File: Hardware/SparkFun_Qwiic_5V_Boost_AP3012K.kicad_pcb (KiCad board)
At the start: 2 copper layers, 25.4 x 25.4 mm, 55 parts, among them J1 Qwiic_RA, J2 Qwiic_RA, J3 Conn_01x06, Q1 BSS138, Q2 BSS138, U5 AP3012

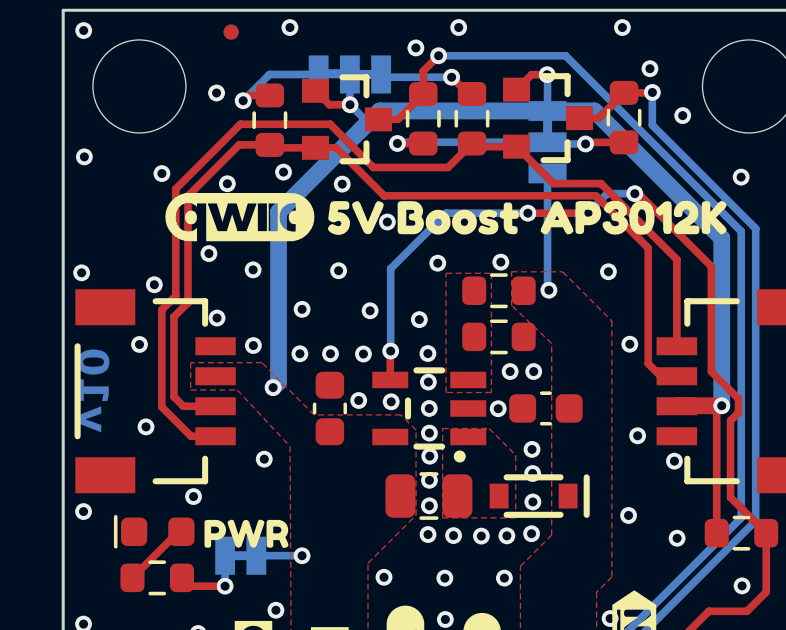
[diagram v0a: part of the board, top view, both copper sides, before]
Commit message: silk adjustments - add flame logo to top
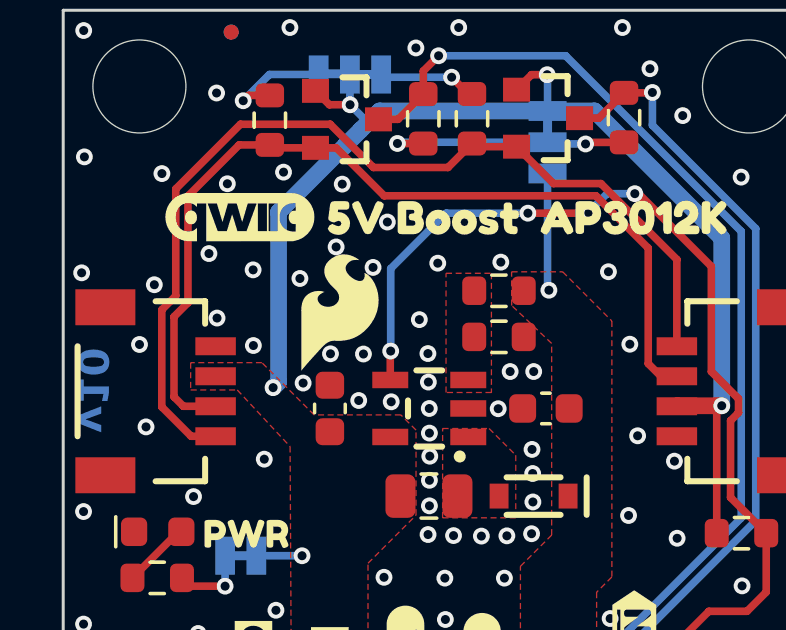
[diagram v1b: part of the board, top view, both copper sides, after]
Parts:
- added G***: Flame, SparkFun-Aesthetic:SparkFun_Flame_4mm, F.Cu at (114.0, 107.9)
- added kibuzzard-67A51CFE: G***, kibuzzard-67A51CFE, B.Cu at (117.6, 113.8)
- moved G*** 1.08 mm to (117.5, 110.5)
- moved G*** 1.08 mm to (117.6, 108.5)
- moved kibuzzard-67A51507 1.08 mm to (117.4, 112.3)

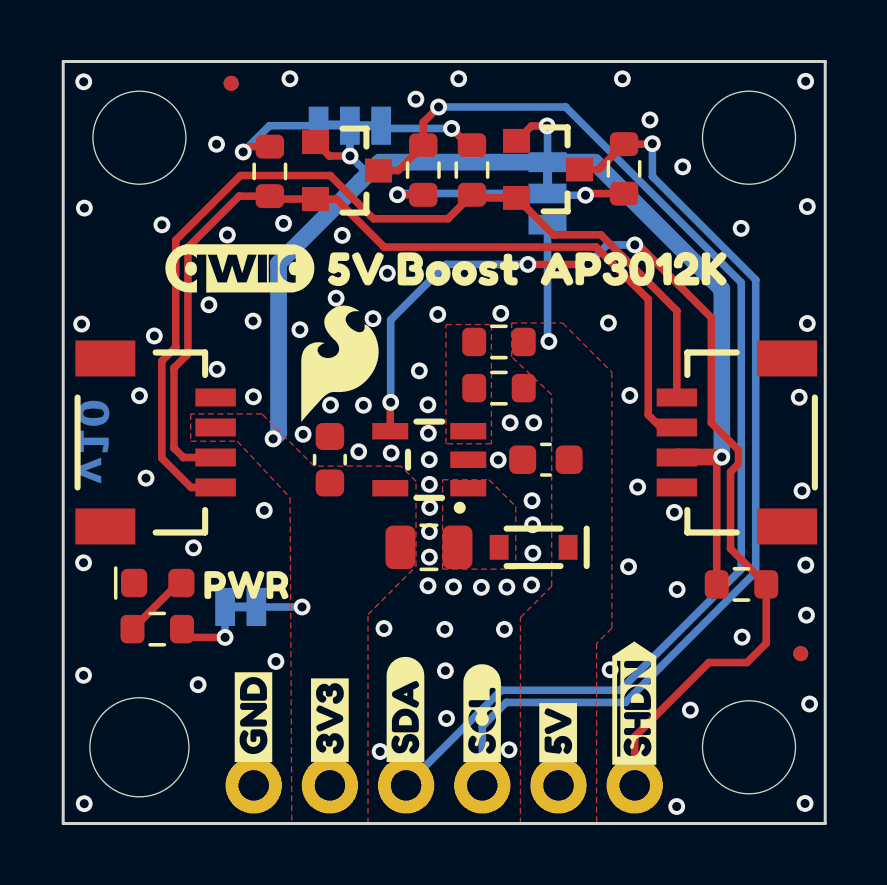
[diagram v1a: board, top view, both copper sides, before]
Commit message: checklist run eng
-sch cleanup
-changed red led bias resistor to 4.7k
-adjusted thermal reliefs/spokes on power PTH headers (GND, 3V3, 5V)
-wire stubs removed
-dimensions added
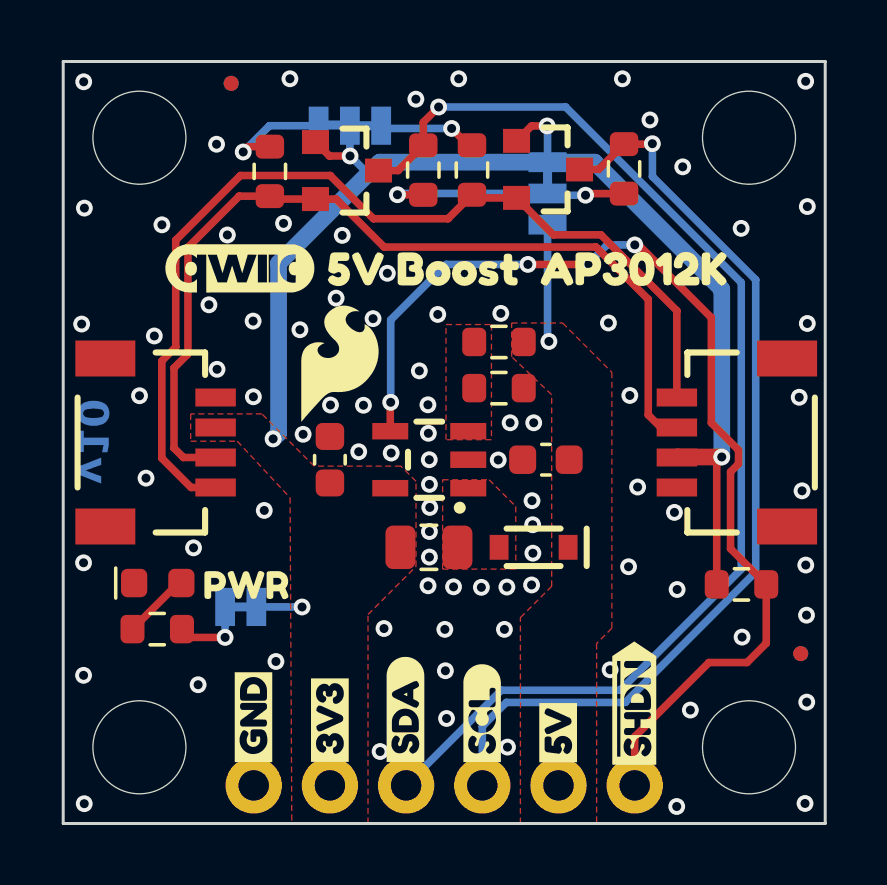
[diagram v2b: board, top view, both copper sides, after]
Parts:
- R3: value 10k -> 4.7k

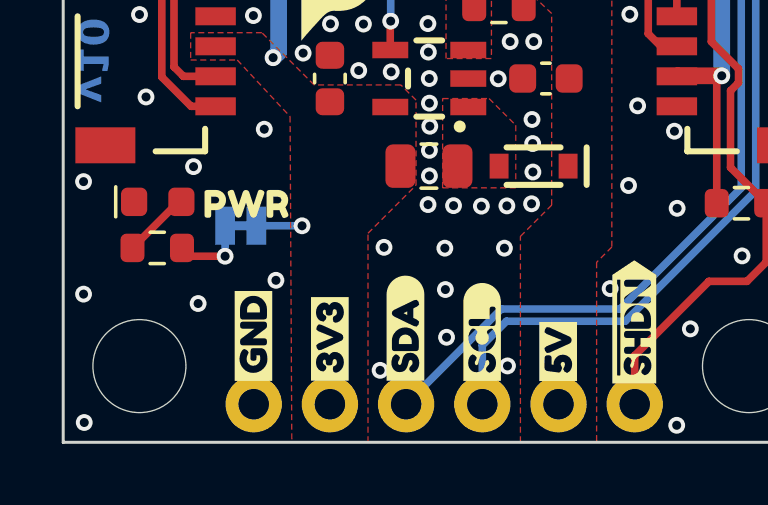
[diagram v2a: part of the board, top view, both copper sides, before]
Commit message: design review changes part 1
-changed silk for logic jumper to PTH LOGIC LEVEL
-Added dashed lines around ADS/SCL PHT headers to show these logic levels are set by LOGIC jumper.
-Changed Value of JP3 to LOGIC
-un-bolded sch block title texts, switched to blue color
-aligned PWR silk label with LED perfectly
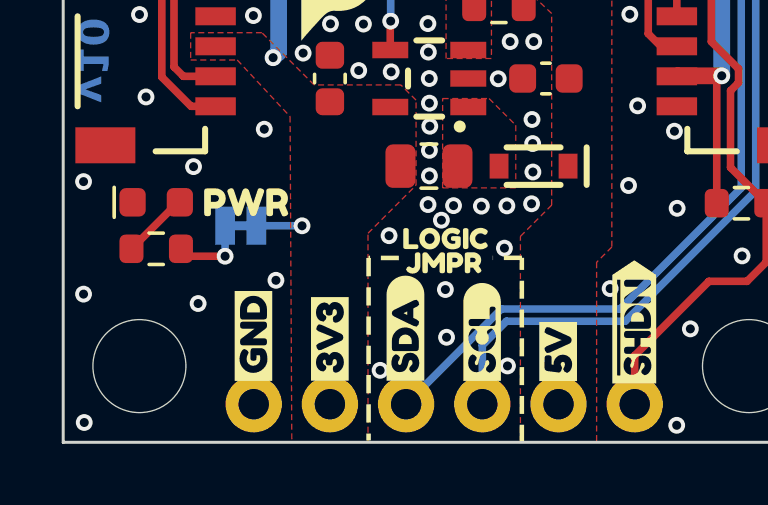
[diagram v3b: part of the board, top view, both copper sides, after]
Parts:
- added kibuzzard-67AB7DC2: G***, kibuzzard-67AB7DC2, F.Cu at (117.5, 116.4)
- added kibuzzard-67AB7DD0: G***, kibuzzard-67AB7DD0, F.Cu at (117.5, 117.2)
- added kibuzzard-67AB7F1B: G***, kibuzzard-67AB7F1B, B.Cu at (119.3, 102.2)
- added kibuzzard-67AB7F2D: G***, kibuzzard-67AB7F2D, B.Cu at (117.5, 102.2)
- JP3: value VOLT -> LOGIC
- moved kibuzzard-67A51B2D 0.90 mm to (118.4, 102.2)
- moved kibuzzard-65A8A8B4 0.05 mm to (110.9, 115.2)
- moved D1 0.05 mm to (107.9, 115.2)

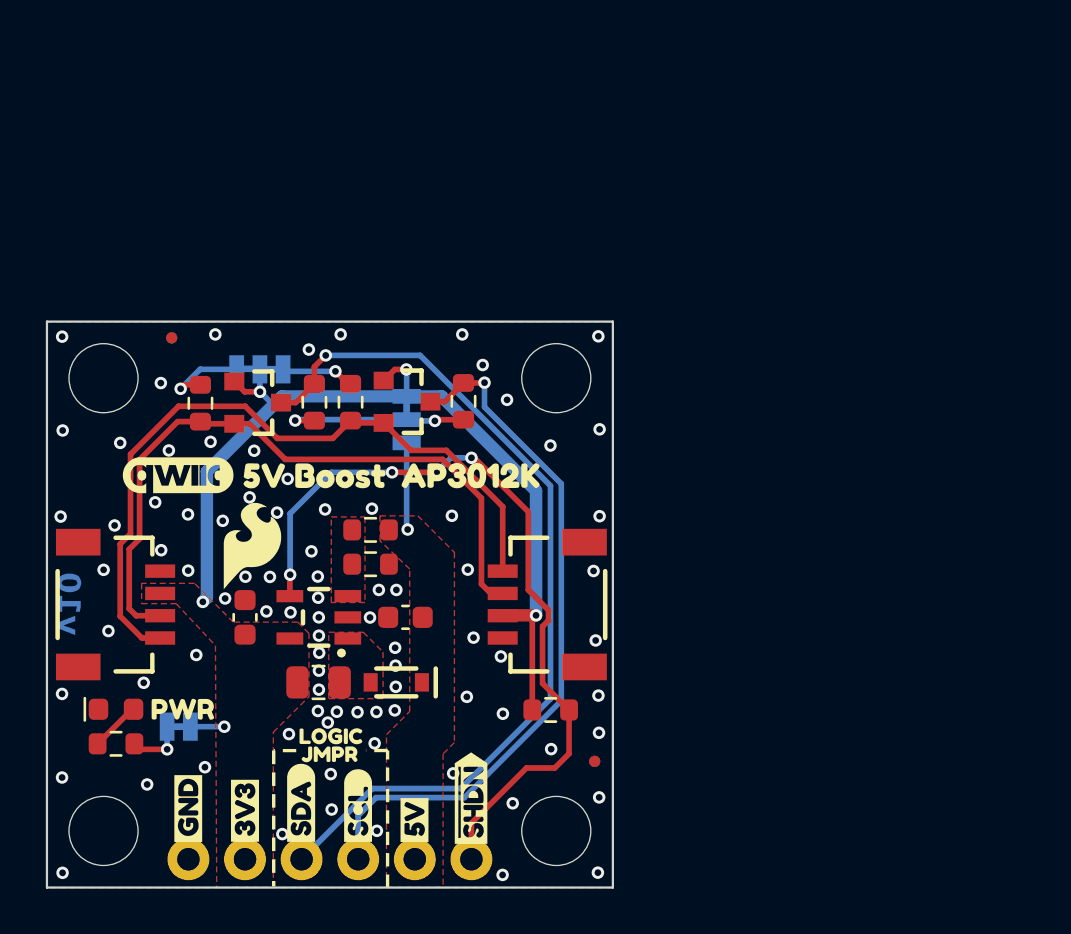
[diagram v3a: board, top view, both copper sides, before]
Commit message: Review part 2
-Update layer names
-changed material to TG135
-Centered (roughly) the board design in the frame
-set my grid/drill origin points to bottom left corner of PCB edge cut (aka dimensional outline).
-updated measures
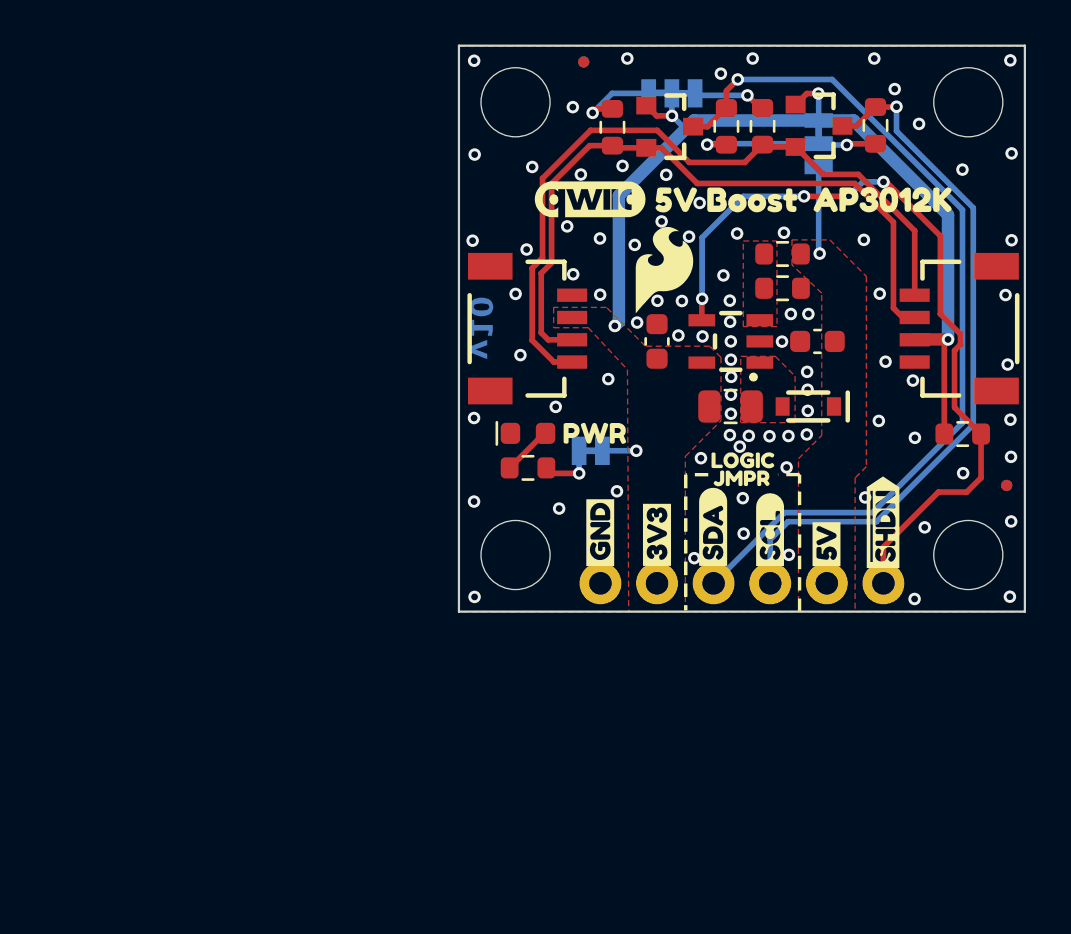
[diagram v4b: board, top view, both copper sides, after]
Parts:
- moved FID2 22.3 mm to (128.9, 86.1)
- moved FID3 22.3 mm to (128.9, 86.1)
- moved G*** 22.3 mm to (132.5, 95.5)
- moved J3 22.3 mm to (129.6, 109.5)
- moved JP2 22.3 mm to (132.8, 87.5)
- moved Q2 22.3 mm to (132.7, 89.0)
- moved R8 22.3 mm to (142.0, 89.0)
- moved kibuzzard-65A8A8B4 22.3 mm to (129.4, 102.8)
- moved kibuzzard-67A5185F 22.3 mm to (137.2, 107.1)
- moved kibuzzard-67A51A0B 22.3 mm to (137.2, 107.1)
- moved kibuzzard-67AB7DD0 22.3 mm to (136.0, 104.8)
- moved C2 22.3 mm to (139.4, 98.7)
- moved D1 22.3 mm to (126.4, 102.8)
- moved D2 22.3 mm to (138.9, 101.6)
- moved G*** 22.3 mm to (129.2, 92.3)
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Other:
- board text added: "Material: TG135"
- board text removed: "Material: TG155"

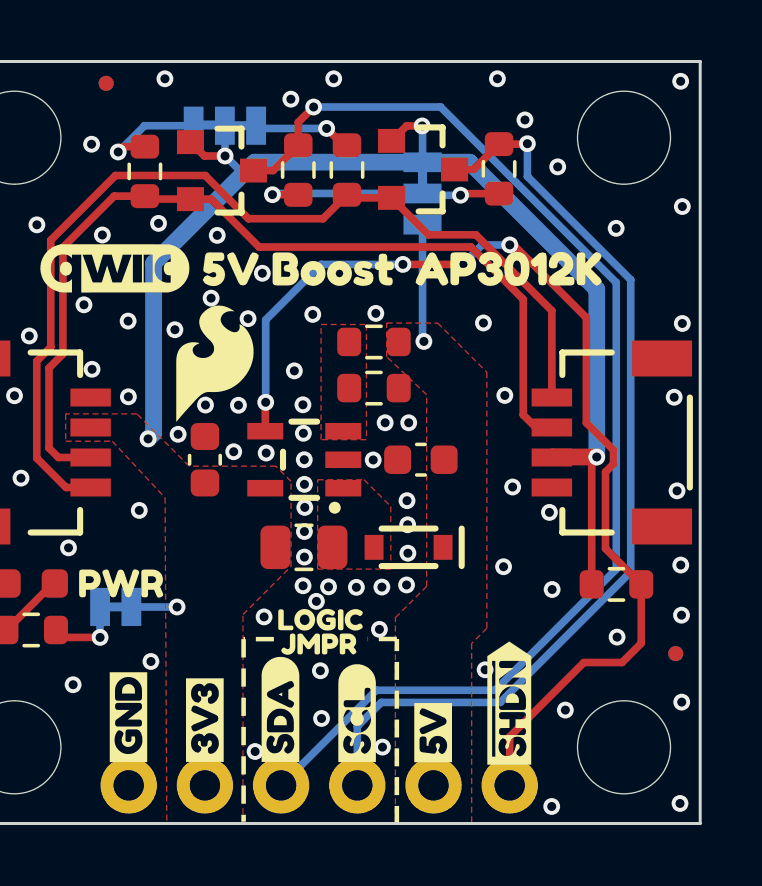
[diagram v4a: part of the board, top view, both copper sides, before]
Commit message: more design review feedback
-SCH, changed all flags to inputs
-BRD, re-routed HV I2C lines to avoid coupling with 3V3 trace
-BRD, adjusted 5V and SHDN routing for less vias/more-direct
-BRD, adjusted SDA/SCL routing away from right qwiic connector to provide more clearance from mask.
-BRD, removed and moved GND vias to avoid bottom silk
-BRD, scooted GND vias near SDA/SCL header pins to avoid bulging in the pours.
-BRD, updated layers to new standards
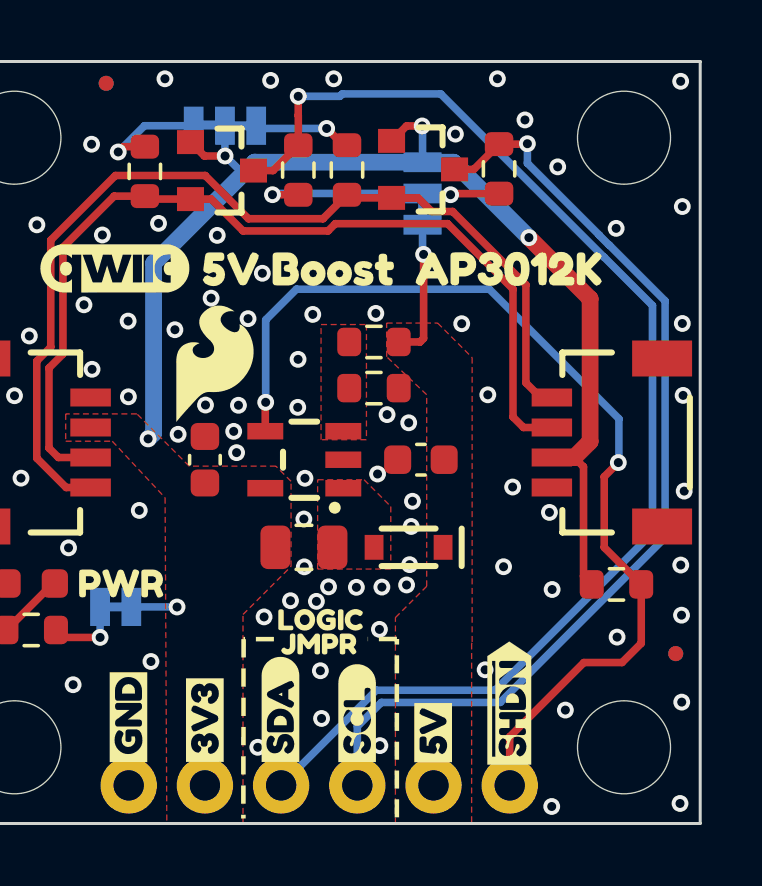
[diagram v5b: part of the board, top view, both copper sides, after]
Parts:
- turned JP3 to 90 degrees
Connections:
- JP3 pad 1: 3.3V -> 5V
- JP3 pad 3: 5V -> 3.3V
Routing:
- net ~{SHDN}: track 35.6 -> 33.2 mm, vias 4 -> 2
- net 3.3V: track 44.0 -> 41.7 mm
- net HV_SDA: track 39.6 -> 41.7 mm
- net HV_SCL: track 31.7 -> 32.6 mm
- net 5V: track 3.91 -> 4.68 mm
- net GND: vias 85 -> 83

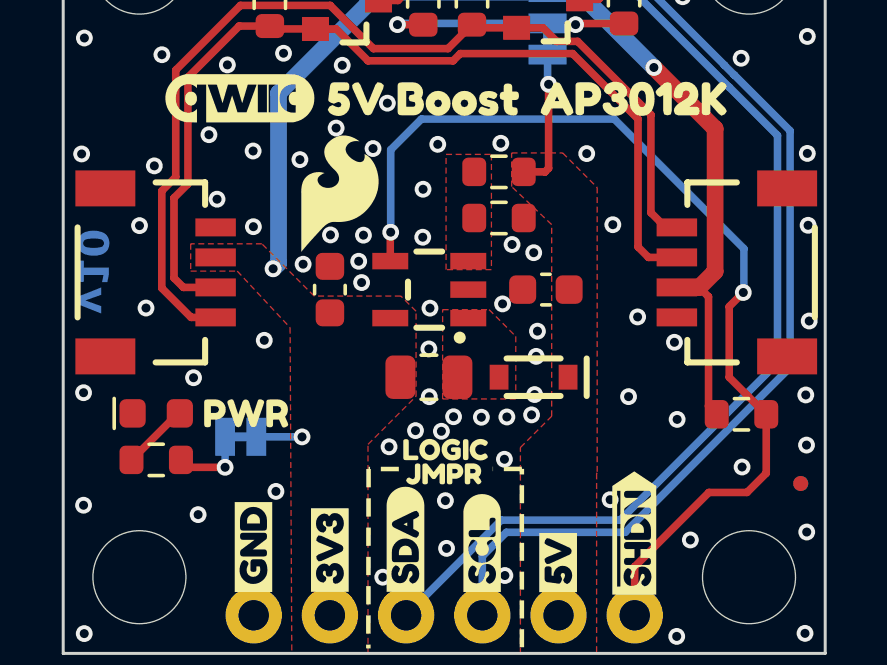
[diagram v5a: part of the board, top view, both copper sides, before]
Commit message: silk update logic level labels
-added 3v3 logic level labels to qwiic connectors
-changed PTH header silk to show default 5V logic level
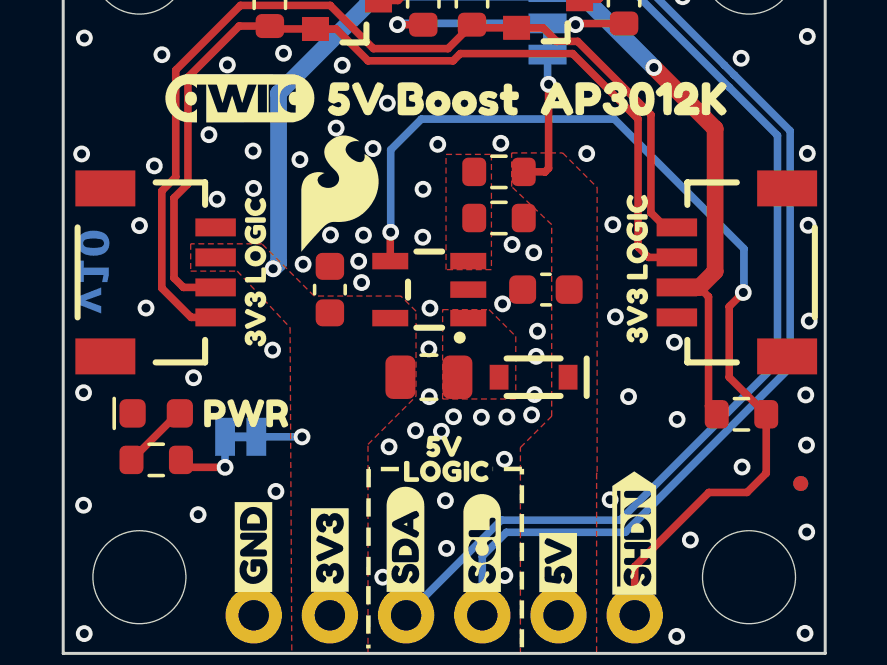
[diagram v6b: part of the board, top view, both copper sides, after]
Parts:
- removed kibuzzard-67AB7DC2: G***, kibuzzard-67AB7DC2
- removed kibuzzard-67AB7DD0: G***, kibuzzard-67AB7DD0
- added kibuzzard-67BF5EEE: G***, kibuzzard-67BF5EEE, F.Cu at (136.0, 103.9)
- added kibuzzard-67BF5EEE: G***, kibuzzard-67BF5EEE, B.Cu at (136.0, 103.9)
- added kibuzzard-67BF5EF7: G***, kibuzzard-67BF5EF7, F.Cu at (136.0, 104.7)
- added kibuzzard-67BF5EF7: G***, kibuzzard-67BF5EF7, B.Cu at (136.0, 104.7)
- added kibuzzard-67BF5F1D: G***, kibuzzard-67BF5F1D, F.Cu at (129.7, 98.1)
- added kibuzzard-67BF5F1D: G***, kibuzzard-67BF5F1D, F.Cu at (142.4, 98.0)
